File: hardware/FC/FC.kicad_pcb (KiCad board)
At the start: 2 copper layers, 52 parts, among them CN1 HC-0.8-8PWT, J1 USB-C, SW1 TS-1088-AR02016, SW2 TS-1088-AR02016, U1 STM32F722RET6, U2 TPS63070RNMR, U4 ICM-20602, U5 AP2112K-3.3TRG1, U6 BMP580, X1 X322525MOB4SI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

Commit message: added pcb design
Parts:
- added H1: MountingHole, MountingHole:MountingHole_2.2mm_M2, F.Cu at (131.2, 115.5)
- added H2: MountingHole, MountingHole:MountingHole_2.2mm_M2, F.Cu at (131.2, 86.5)
- added H3: MountingHole, MountingHole:MountingHole_2.2mm_M2, F.Cu at (179.2, 86.5)
- added H4: MountingHole, MountingHole:MountingHole_2.2mm_M2, F.Cu at (179.2, 115.5)
- moved C24 34.1 mm to (134.0, 104.2), turned to 180 degrees
- moved C25 30.2 mm to (134.0, 102.0), turned to 180 degrees
- moved C14 28.1 mm to (168.2, 101.3), turned to -90 degrees
- moved C13 27.6 mm to (166.8, 101.3), turned to 90 degrees
- moved C26 27.4 mm to (134.0, 99.5)
- moved C8 26.7 mm to (174.2, 115.8), turned to 0 degrees
- moved C27 26.2 mm to (134.1, 97.0)
- moved C12 26.1 mm to (165.0, 101.3), turned to 90 degrees
- moved C4 23.7 mm to (170.0, 114.0), turned to 90 degrees
- moved R2 23.1 mm to (145.2, 92.8)
- moved C20 22.0 mm to (157.7, 112.5), turned to 180 degrees
- moved C21 21.4 mm to (157.7, 110.8), turned to 180 degrees
- moved C7 21.3 mm to (163.8, 114.0)
- moved C6 21.0 mm to (167.5, 114.0), turned to 90 degrees
- moved C22 20.4 mm to (157.7, 109.0), turned to 180 degrees
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- renumbered +V to +V1, GND to GND1
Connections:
- C28 pad 2: Net-(X1-OSC1) -> /HSE_IN
- C29 pad 1: Net-(X1-OSC2) -> GND
- C29 pad 2: GND -> /HSE_OUT
- J1 pad A4B9: VBUS -> +3V3
- J1 pad A8: /SBU1 -> unconnected-(J1-SBU1-PadA8)
- J1 pad B4A9: VBUS -> +3V3
- J1 pad B8: /SBU2 -> unconnected-(J1-SBU2-PadB8)
- U1 pad 15: unconnected-(U1-PA1-Pad15) -> /ESC_TELE
- U1 pad 20: /ICM_CS -> /ICM_INT
- U1 pad 21: /ICM_SCK -> /ICM_CS
- U1 pad 24: unconnected-(U1-PC4-Pad24) -> /ICM_SCK
- U1 pad 44: /USB_D1- -> /USB_D1+
- U1 pad 45: /USB_D1+ -> /USB_D1-
- U1 pad 5: GND -> /HSE_IN
- U1 pad 51: /ESC_TELE -> unconnected-(U1-PC10-Pad51)
- U1 pad 6: GND -> /HSE_OUT
- X1 pad 1: Net-(X1-OSC1) -> /HSE_IN
- X1 pad 3: Net-(X1-OSC2) -> /HSE_OUT
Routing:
- net +3V3: track 0.00 -> 121.0 mm, vias 0 -> 8
- net GND: track 0.00 -> 81.9 mm, vias 0 -> 63
- net +5V: track 0.00 -> 46.0 mm, vias 0 -> 2
- net /VSYS: track 0.00 -> 31.9 mm
- net /ESC_CURR: track 0.00 -> 25.7 mm, vias 0 -> 2
- net /ESC_TELE: track 0.00 -> 25.0 mm, vias 0 -> 2
- net /ESC1: track 0.00 -> 18.9 mm
- net /ESC2: track 0.00 -> 18.7 mm
- net /ESC3: track 0.00 -> 18.5 mm
- net /ESC4: track 0.00 -> 18.3 mm
- net /RESET: track 0.00 -> 16.7 mm, vias 0 -> 2
- net /BOOT: track 0.00 -> 13.4 mm
- net /HSE_OUT: track 0.00 -> 10.4 mm
- net /I2C_SCL: track 0.00 -> 9.91 mm, vias 0 -> 2
- net /ICM_INT: track 0.00 -> 8.84 mm, vias 0 -> 2
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- added copper zone on F.Cu, net +3V3
- added copper zone on F.Cu, net /VSYS
- added copper zone on B.Cu, net GND
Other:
- board outline added: 54.5 x 35.5 mm

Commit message: added LED for PS
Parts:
- added D1: LED, Diode_SMD:D_0805_2012Metric_Pad1.15x1.40mm_HandSolder, F.Cu at (136.2, 92.8)
- added G***: LOGO, GRAPHIC:GRAPHIC_V2, F.Cu at (173.5, 92.0)
- added R8: 150, Resistor_SMD:R_0603_1608Metric_Pad0.98x0.95mm_HandSolder, F.Cu at (136.2, 89.5)
- added REF**: radio_solder_pads, RADIO_SOLDER_PADS:radio_solder_pads, F.Cu at (153.5, 117.5)
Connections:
- U1 pad 53: unconnected-(U1-PC12-Pad53) -> /RADIO_TX
- U1 pad 54: unconnected-(U1-PD2-Pad54) -> /RADIO_RX
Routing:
- net /RADIO_TX: track 0.00 -> 29.6 mm, vias 0 -> 2
- net /RADIO_RX: track 0.00 -> 26.1 mm, vias 0 -> 2
- net +5V: track 46.0 -> 57.2 mm
- net +3V3: track 121.0 -> 129.5 mm
- net GND: track 81.9 -> 88.4 mm, vias 63 -> 65
- net Net-(D1-A): track 0.00 -> 3.30 mm
- added copper zone on F.Cu, net GND

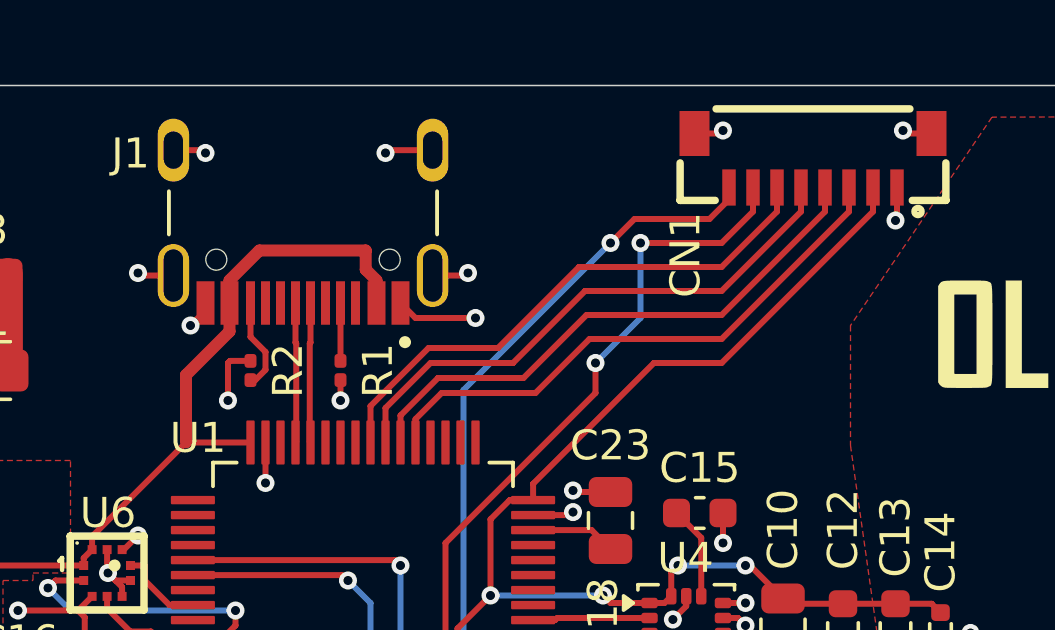
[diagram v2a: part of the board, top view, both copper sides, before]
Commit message: fixed vbus line, added diode and graphic
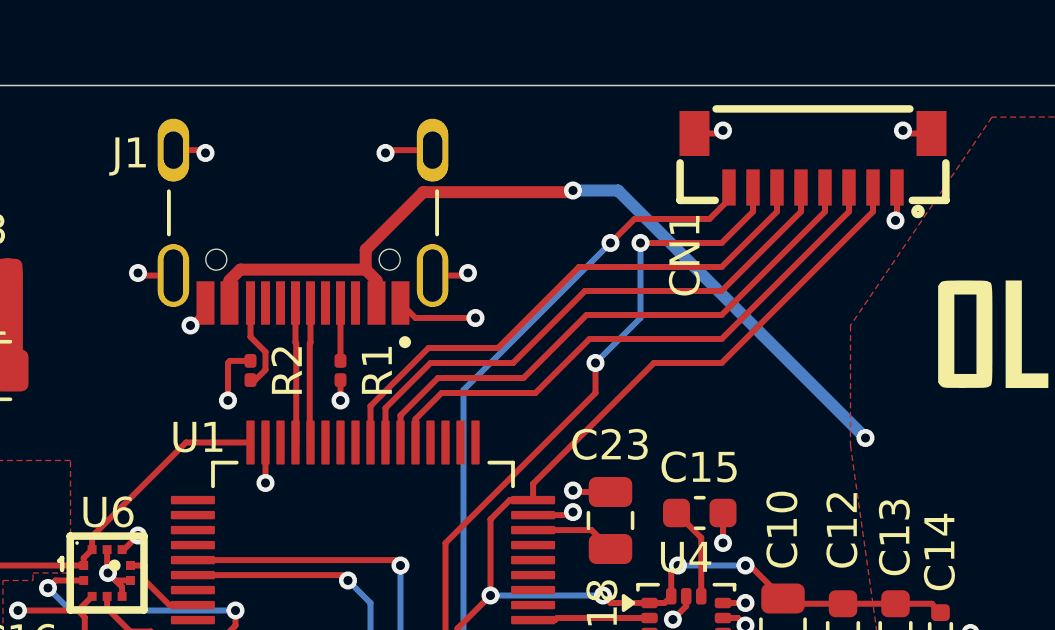
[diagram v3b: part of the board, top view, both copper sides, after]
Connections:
- +V1 pad 1: /VSYS -> VBUS
- C1 pad 1: /VSYS -> VBUS
- C2 pad 1: /VSYS -> VBUS
- C3 pad 1: /VSYS -> VBUS
- J1 pad A4B9: +3V3 -> VBUS
- J1 pad B4A9: +3V3 -> VBUS
- R3 pad 1: /VSYS -> VBUS
- U2 pad 12_13: /VSYS -> VBUS
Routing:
- net VBUS: track 0.00 -> 60.2 mm, vias 0 -> 2
- net /VSYS: track 31.9 -> 0.00 mm
- net +3V3: track 129.5 -> 116.6 mm
- added copper zone on F.Cu, net VBUS
- removed copper zone on F.Cu, net /VSYS
